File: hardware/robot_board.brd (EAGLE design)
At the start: 92.7 x 72.1 mm, 113 parts, among them J1 POWER_JACKPTH, U2 FT232RLSSOP

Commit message: check in library and restructured directories
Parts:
- removed U$4: MC74HC164, r_cubed:TSSOP-14
- removed U2: FT232RLSSOP, SparkFun-DigitalIC:SSOP28DB
- added R45, R46: (no value), resistor:R1206
- added U1: FT232RL-BASICSSOP, SparkFun-DigitalIC:SSOP28DB
- moved D24 2.84 mm to (33.0, 22.9)
- turned U17 to 270 degrees
- renumbered U$13 to U13, U$14 to U14, U$15 to U15, U$16 to U16, U$17 to U17, U$18 to U18, U$5 to U5, U$6 to U6
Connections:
- removed net N$28: U$4.9
- removed net N$29: U$4.1, U$4.2
- removed net N$32: U$4.8
- removed net V+: U$12.8
- removed net VCC: U2.20
- new net AOUT1: U$19.L, U$21.2
- new net AOUT2: U$19.R, U$21.4
- new net BOUT1: U$20.L, U$21.7
- new net BOUT2: U$20.R, U$21.5
- new net GND1: U1.7
- new net GND2: U1.18
- new net GND3: U1.21
- new net MAIN_PWR: C3.+, D25.A, JP6.1, JP6.2, JP6.3, JP6.4, R27.1, R31.2, U$3.P$1, U$3.P$3, U$9.2, U13.P$5, U13.P$6, U16.8, U5.P$4, U6.P$4
- new net N$52: R45.1, R46.2, U17.55
- net 5V: now also U13.P$1; no longer C3.+, D25.A, JP6.1, JP6.2, JP6.3, JP6.4, R27.1, R31.2, U$11.8, U$3.P$1, U$3.P$3, U$4.14, U$9.2, U13.P$5, U16.8, U5.P$4, U6.P$4
- net AGND: now also U1.25; no longer U2.25
- net GND: now also R46.1, U16.5, U16.6; no longer U$4.7, U2.18, U2.21, U2.7
- net LCD0: no longer U$4.3
- net LCD1: no longer U$4.4
- net LCD2: no longer U$4.5
- net LCD3: no longer U$4.6
- net LCD4: no longer U$4.10
- net LCD5: no longer U$4.11
- net LCD6: no longer U$4.12
- net LCD7: no longer U$4.13
- net N$1: now also U1.16; no longer U2.16
- net N$2: now also U1.15; no longer U2.15
- net USB_5V: now also U1.20
- net VCCIO: now also U1.4; no longer U2.4
- net VIN_F: now also R33.2, R45.2, U$11.8, U$12.8
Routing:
- net MAIN_PWR: track 0.00 -> 7.62 mm
- net 5V: track 7.62 -> 0.00 mm
- net N$29: track 0.63 -> 0.00 mm

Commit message: updated schematic
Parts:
- removed U$10: 1206PPTC_FUSE, jseng:R1206
- removed U15: DMP2035U, jseng:SOT23
- added D26, D27, D28, D29: (no value), SparkFun-DiscreteSemi:SOT23-3
- added F2: 1206PPTC_FUSE, jseng:R1206
- added R47, R48, R49, R50: 220, resistor:R1206
- added U2: NCP380, jseng:TSOP-5
- R30, R31, R32, R33, R34, R42: value (none) -> 10K
- U$2: value NCP380 -> SIA907EDJT; device jseng:TSOP-5 -> jseng:SC70T
- moved U$2 22.9 mm to (8.89, 21.6), turned to 0 degrees
- moved R43 12.5 mm to (35.6, 52.1), turned to 90 degrees
- moved JP3 5.08 mm to (10.2, 62.2)
- moved JP7 5.08 mm to (10.2, 67.3)
- moved U13 2.54 mm to (8.89, 15.2)
- moved U1 2.54 mm to (16.5, 45.7)
- moved F1 1.80 mm to (19.1, 34.3)
- moved U18 1.80 mm to (27.9, 50.8), turned to 180 degrees
- moved U17 1.27 mm to (68.6, 36.8)
- renumbered U$12 to U12, U$3 to U3, U$7 to U7, U$8 to U8
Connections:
- removed net AGND: U1.25
- removed net GND1: U1.7
- removed net GND2: U1.18
- removed net GND3: U1.21
- new net N$28: U$2.P$3, U$2.P$6
- new net N$29: D26.3, R47.1
- new net N$32: D27.3, R48.1
- new net N$53: D28.3, R49.1
- new net N$54: D29.3, R50.1
- new net SERVO0: JP3.1, R47.2
- new net SERVO1: JP3.2, R48.2
- new net SERVO2: JP3.3, R49.2
- new net SERVO3: JP3.4, R50.2
- net 5V: now also U13.P$10, U2.P$4, U2.P$6; no longer U$2.P$4, U$2.P$6
- net 5V_UC: now also U2.P$1; no longer U$2.P$1
- net GND: now also D26.1, D27.1, D28.1, D29.1, U1.18, U1.21, U1.25, U1.7, U2.P$5; no longer U$2.P$5
- net MAIN_PWR: now also U13.P$7, U13.P$8
- net N$27: now also F2.1; no longer U$10.1
- net N$31: now also U2.P$2; no longer U$2.P$2
- net USBGATE: now also U$2.P$2, U$2.P$5; no longer U15.1
- net USB_5V: now also F2.2, U$2.P$1; no longer U$10.2, U15.3
- net VIN_F: now also U$2.P$4; no longer U15.2
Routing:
- net MAIN_PWR: track 7.62 -> 0.00 mm
- net GND: track 16.7 -> 9.05 mm
- net N$26: track 2.80 -> 0.21 mm

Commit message: update libraries
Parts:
- removed U$21: DRV8833, jseng:TSSOP16
- added U$3: NRSINDUCTOR, jseng:TAIYO-NRS
- added U$4, U$5: DRV8839, jseng:PWSON-N12
- moved R34 10.2 mm to (20.3, 12.7), turned to 90 degrees
- moved R47 6.35 mm to (3.81, 57.1)
- moved U$20 5.08 mm to (22.9, 64.8), turned to 180 degrees
- moved R48 5.08 mm to (7.62, 57.1)
- moved U$19 5.08 mm to (33.0, 64.8), turned to 180 degrees
- moved R49 3.81 mm to (11.4, 57.1)
- moved R50 2.54 mm to (15.2, 57.1)
- moved R42 1.27 mm to (16.5, 12.7)
- moved U13 1.27 mm to (8.89, 16.5)
- moved R29 1.27 mm to (11.4, 25.4)
- moved U$2 1.27 mm to (8.89, 22.9)
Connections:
- new net N$55: U$3.P$2, U13.P$2
- new net N$56: U$3.P$1, U13.P$4
- new net N$58: U$4.P$1, U$4.P$2
- new net N$61: U$5.P$1, U$5.P$2
- net 5V: now also U$4.P$7, U$4.P$8, U$5.P$7, U$5.P$8
- net AOUT1: now also U$4.P$3; no longer U$21.2
- net AOUT2: now also U$4.P$4; no longer U$21.4
- net BOUT1: now also U$5.P$3; no longer U$21.7
- net BOUT2: now also U$5.P$4; no longer U$21.5
- net GND: now also U$4.P$5, U$4.P$6, U$5.P$5, U$5.P$6; no longer U$21.13

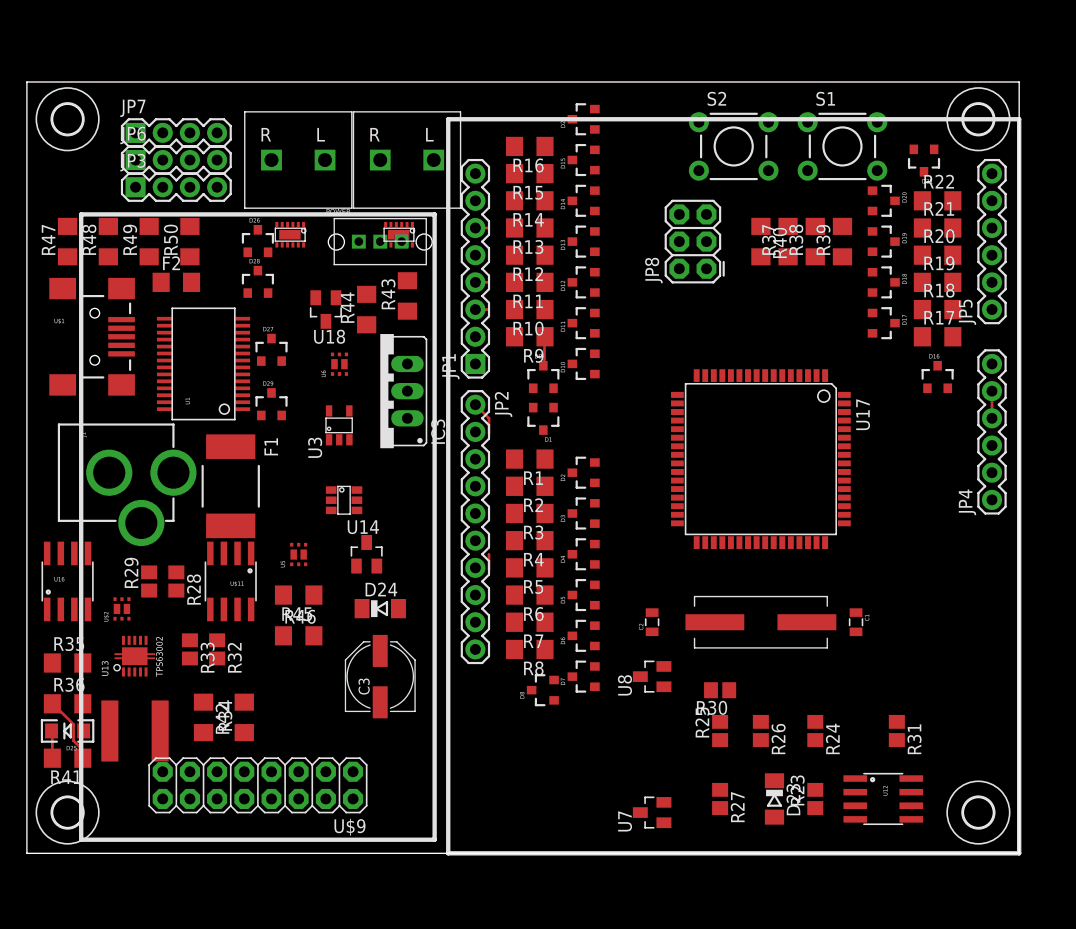
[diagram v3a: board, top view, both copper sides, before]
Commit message: added accelerometer device
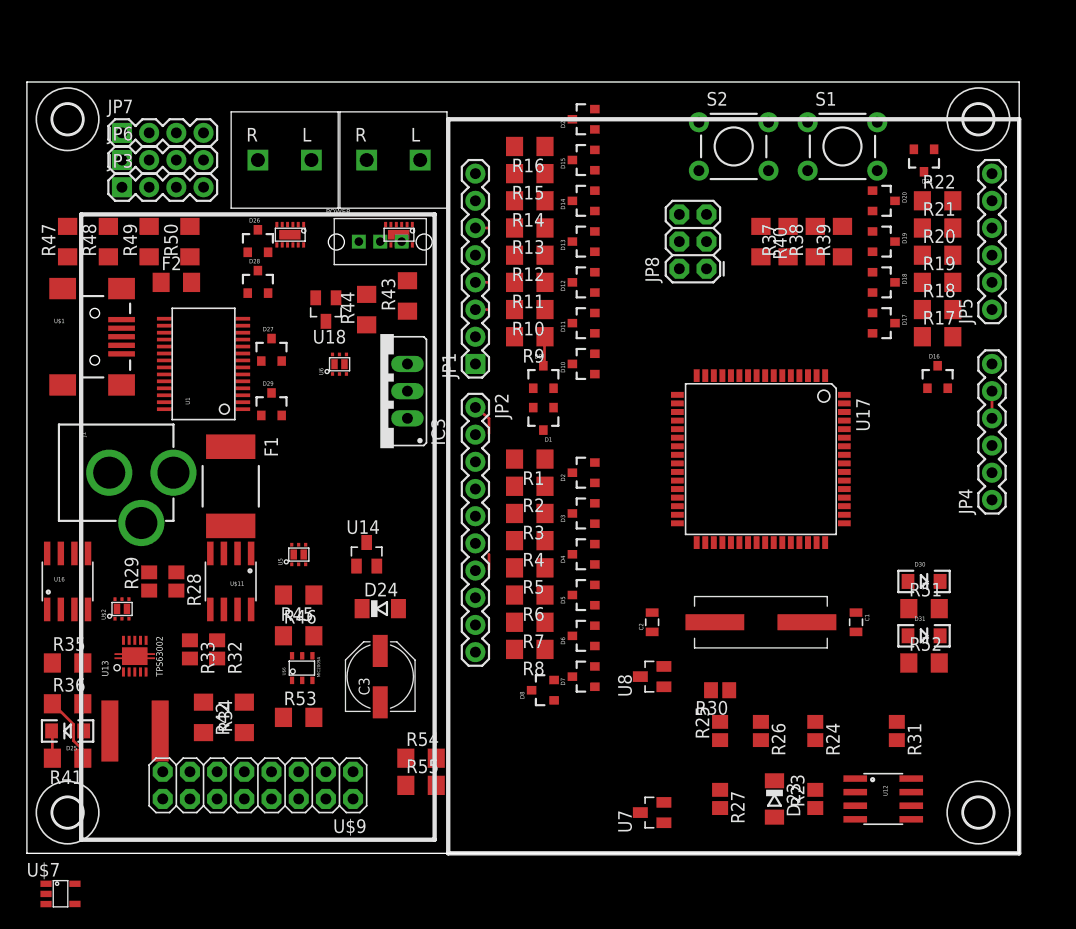
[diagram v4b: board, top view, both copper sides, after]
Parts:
- removed U2: NCP380, jseng:TSOP-5
- removed U3: TLV70233DBVR, jseng:SOT-23-5
- added D30: GREEN, SparkFun-LED:LED-1206
- added D31: YELLOW, SparkFun-LED:LED-1206
- added R51, R52: 330, resistor:R1206
- added R53: 1.5K, resistor:R1206
- added R54: 10K, resistor:R1206
- added R55: 1K, resistor:R1206
- added U$6: MIC2009A, jseng:SOT23-M5
- added U$7: TLV70233, jseng:SOT-23-5
- D23: value 2.7V -> 2.1V
- D25: value GREEN -> POWER
- R41: value (none) -> 330
- moved U$19 1.27 mm to (31.8, 64.8)
- moved JP3 1.27 mm to (8.89, 62.2)
- moved JP6 1.27 mm to (8.89, 64.8)
- moved JP7 1.27 mm to (8.89, 67.3)
- moved U$20 1.27 mm to (21.6, 64.8)
- moved JP2 0.25 mm to (41.9, 41.7)
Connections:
- net 10 renamed D10
- net 11 renamed D11
- net 12 renamed D12
- net 13 renamed D13
- net 2.7V renamed 2.1V
- net 8 renamed D8
- net 9 renamed D9
- net N$20 renamed D7_IN
- net N$29 renamed SERVO0_IN
- net N$32 renamed SERVO1_IN
- net N$5 renamed D8_IN
- net N$53 renamed SERVO2_IN
- net N$54 renamed SERVO3_IN
- net N$6 renamed D9_IN
- removed net N$10: D6.3, R6.1
- removed net N$11: D7.3, R7.1
- removed net N$12: D8.3, R8.1
- removed net N$13: D9.3, R9.1
- removed net N$14: D10.3, R10.1
- removed net N$15: D11.3, R11.1
- removed net N$16: D12.3, R12.1
- removed net N$17: D13.3, R13.1
- removed net N$18: D14.3, R14.1
- removed net N$19: D15.3, R15.1
- removed net N$21: D16.3, R17.1
- removed net N$22: D17.3, R18.1
- removed net N$23: D18.3, R19.1
- removed net N$24: D19.3, R20.1
- removed net N$25: D20.3, R21.1
- removed net N$26: D21.3, R22.1
- removed net N$31: U2.P$2
- removed net N$58: U$4.P$1, U$4.P$2
- removed net N$61: U$5.P$1, U$5.P$2
- removed net N$7: D3.3, R3.1
- removed net N$8: D4.3, R4.1
- removed net N$9: D5.3, R5.1
- new net A0_IN: D16.3, R17.1, U17.61
- new net A1_IN: D17.3, R18.1, U17.60
- new net A2_IN: D18.3, R19.1, U17.59
- new net A3_IN: D19.3, R20.1, U17.58
- new net A4_IN: D20.3, R21.1, U17.57
- new net A5_IN: D21.3, R22.1, U17.56
- new net D0_IN: D9.3, R9.1, U17.2
- new net D1_IN: D10.3, R10.1, U17.3
- new net D2_IN: D11.3, R11.1, U17.4
- new net D3_IN: D12.3, R12.1, U17.5
- new net D4_IN: D13.3, R13.1, U17.8
- new net D5_IN: D14.3, R14.1, U17.15
- new net D6_IN: D15.3, R15.1, U17.16
- new net LED0: D30.A, U17.33
- new net LED1: D31.A, U17.34
- new net M0_DIR0: U$4.P$9, U17.29
- new net M0_DIR1: U$4.P$11, U17.30
- new net M0_EN: U$4.P$10, U$4.P$12, U17.14
- new net M1_DIR0: U$5.P$9, U17.31
- new net M1_DIR1: U$5.P$11, U17.32
- new net M1_EN: U$5.P$10, U$5.P$12, U17.17
- new net N$5: R53.2, U$6.P$5
- new net N$57: D30.C, R51.2
- new net N$6: R55.2, U17.43
- new net N$62: D31.C, R52.2
- new net SCL_IN: D7.3, R7.1, U17.6
- new net SDA_IN: D8.3, R8.1, U17.7
- new net SS: D3.3, R3.1, U17.10
- net 3V3: now also U$7.P$4; no longer U3.P$4
- net 5V: now also U$6.P$1; no longer U2.P$4, U2.P$6
- net 5V_UC: no longer U2.P$1
- net A0: no longer U17.61
- net A1: no longer U17.60
- net A2: no longer U17.59
- net A3: no longer U17.58
- net A4: no longer U17.57
- net A5: no longer U17.56
- net AREF: now also U17.62
- net D0: no longer U17.2
- net D1: no longer U17.3
- net GND: now also R51.1, R52.1, R53.1, R54.1, U$7.P$2; no longer U2.P$5, U3.P$2
- net HIGH_5V_REG: now also U6.P$6; no longer U6.P$1
- net MAIN_PWR: now also U$7.P$1, U$7.P$3, U5.P$3, U6.P$3; no longer U3.P$1, U3.P$3, U5.P$4, U6.P$4
- net MISO: now also D5.3, R5.1, U17.13
- net MOSI: now also D4.3, R4.1, U17.12
- net N$28: now also U$2.P$1, U$2.P$4; no longer U$2.P$3, U$2.P$6
- net N$42: now also U6.P$1, U6.P$4; no longer U6.P$3, U6.P$6
- net N$44: now also U5.P$1, U5.P$4; no longer U5.P$3, U5.P$6
- net SCK: now also D6.3, R6.1, U17.11
- net USB_5V: now also R54.2, R55.1, U$2.P$6; no longer U$2.P$1
- net VIN_F: now also U$2.P$3, U$4.P$1, U$4.P$2, U$5.P$1, U$5.P$2, U5.P$6; no longer U$2.P$4, U5.P$1
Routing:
- net N$13: track 2.80 -> 0.00 mm
- net D0_IN: track 0.00 -> 2.80 mm

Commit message: changed board size and added gyro interrupt
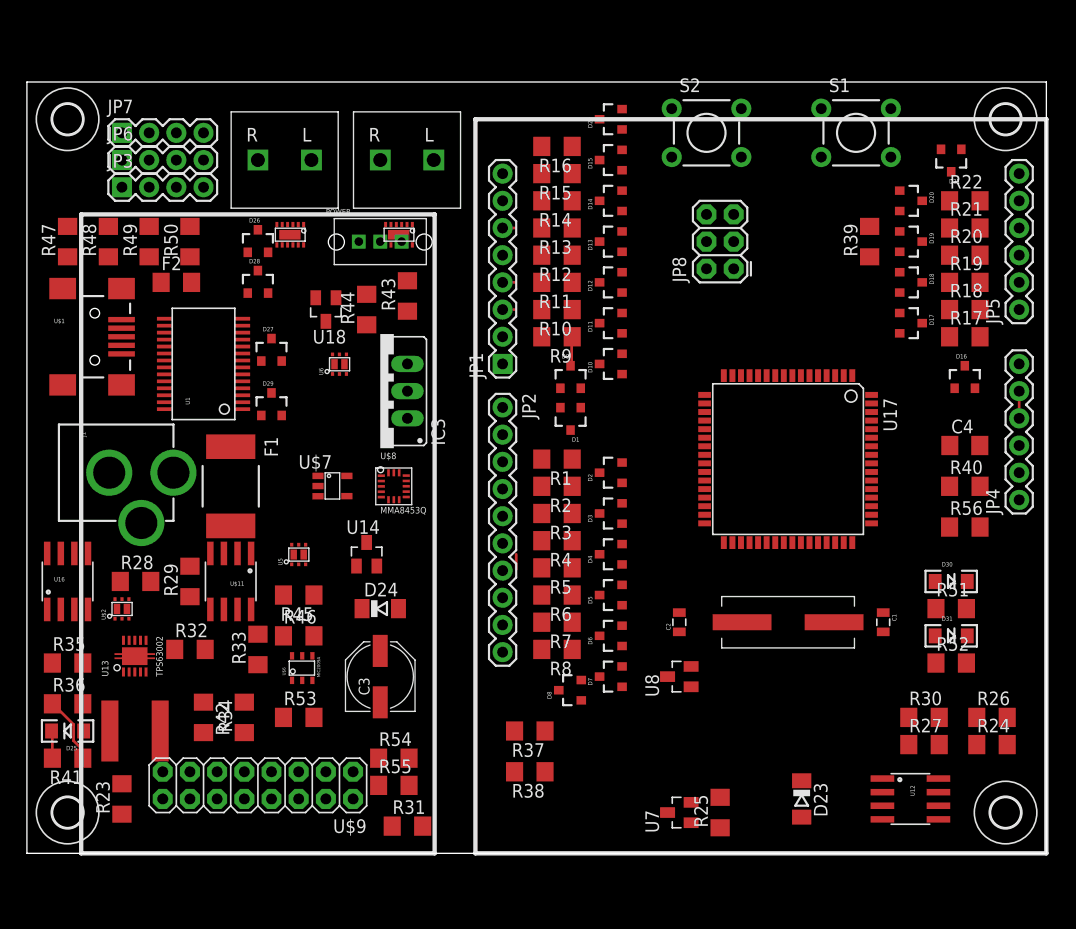
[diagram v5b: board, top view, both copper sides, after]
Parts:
- added C4: .1uF, resistor:C1206
- added R56: 1K, resistor:R1206
- added U$8: MMA8453Q, jseng:QFN-COL
- R23, R24, R25, R26, R27: device resistor:R0805 -> resistor:R1206
- R28: value 86.6K -> (none); device resistor:R0805 -> resistor:R1206
- R29: value 100K -> (none); device resistor:R0805 -> resistor:R1206
- R30, R31, R32, R33: value 10K -> (none); device resistor:R0805 -> resistor:R1206
- R37, R38: value 1k -> 4.7K
- R40: value 1k -> 10K
- moved R23 64.8 mm to (8.89, 5.08)
- moved R38 56.3 mm to (47.0, 7.62), turned to 180 degrees
- moved R37 51.7 mm to (47.0, 11.4), turned to 180 degrees
- moved R31 46.6 mm to (35.6, 2.54), turned to 0 degrees
- moved U$7 45.8 mm to (26.7, 33.0)
- moved R40 29.8 mm to (87.6, 34.3), turned to 0 degrees
- moved R26 21.6 mm to (90.2, 12.7), turned to 0 degrees
- moved R27 19.7 mm to (83.8, 10.2), turned to 0 degrees
- moved R30 19.2 mm to (83.8, 12.7), turned to 0 degrees
- moved R24 16.6 mm to (90.2, 10.2), turned to 0 degrees
- moved R25 7.62 mm to (64.8, 3.81)
- moved R33 6.35 mm to (21.6, 19.1), turned to 90 degrees
- moved R28 3.81 mm to (10.2, 25.4), turned to 0 degrees
- moved R29 3.81 mm to (15.2, 25.4)
- moved S2 2.84 mm to (63.5, 67.3)
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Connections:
- removed net N$37: JP8.4, R40.1
- removed net N$49: JP8.3, R38.2
- removed net N$50: JP8.1, R37.2
- new net DTR: C4.1, U1.2
- new net GYRO_INT: U$8.P$11, U17.26
- new net LCD_E: U17.19
- new net LCD_RS: U17.18
- new net N$7: JP4.1, R56.2
- new net SW1: S2.3, S2.4
- net 2.1V: now also R23.1; no longer R27.2
- net 3V3: now also R37.2, R38.2, U$8.P$1, U$8.P$14, U$8.P$15, U$8.P$16
- net 3V3_OUT: now also R27.2; no longer R24.2
- net 5VREG_SW: now also R33.1; no longer R32.1
- net 5VREG_SWO: now also R32.1; no longer R33.1
- net 5V_OUT: now also R24.2; no longer R26.2
- net 5V_UC: now also R40.1
- net D11: now also JP8.4
- net D12: now also JP8.1
- net D13: now also JP8.3
- net GND: now also R26.1, R28.1, R31.1, S2.1, S2.2, U$8.P$10, U$8.P$12, U$8.P$13, U$8.P$5, U$8.P$7, U$8.P$8; no longer R23.1, R25.1, R29.1
- net LCD0: now also U17.51
- net LCD1: now also U17.50
- net LCD2: now also U17.49
- net LCD3: now also U17.48
- net LCD4: now also U17.47
- net LCD5: now also U17.46
- net LCD6: now also U17.45
- net LCD7: now also U17.44
- net MAIN_PWR: now also R23.2, R25.2; no longer R27.1, R31.2
- net MISO: no longer R37.1
- net MOSI: no longer R40.2
- net N$3: now also U17.23
- net N$30: now also R25.1; no longer R31.1
- net N$34: now also R24.1, R26.2; no longer R25.2, R26.1
- net N$35: now also R28.2, R29.1; no longer R28.1, R29.2
- net N$38: now also R27.1, R31.2; no longer R23.2, R24.1
- net N$4: now also U17.24
- net RESET: now also C4.2, R40.2, R56.1; no longer JP4.1
- net SCK: no longer R38.1
- net SCL_IN: now also R38.1, U$8.P$4
- net SDA_IN: now also R37.1, U$8.P$6
- net VIN_F: now also R29.2; no longer R28.2
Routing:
- net D8: track 3.05 -> 0.00 mm
- net D0: track 0.88 -> 0.00 mm
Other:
- board size 92.7 x 72.1 mm -> 95.2 x 72.1 mm

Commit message: modified overall layout
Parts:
- removed D24: 6V, diode:SOD80C
- removed U$1: USB-MINIB-5PIN, SparkFun-Connectors:USB-MINIB
- removed U$11: LM393, SparkFun-AnalogIC:SO08
- removed U$3: NRSINDUCTOR, jseng:TAIYO-NRS
- removed U13: TPS63002, jseng:10SON
- removed U14, U18: DMP2035U, jseng:SOT23
- removed U7, U8: DMP2035U-7, jseng:SOT23
- added C5: .1uF, resistor:C1206
- added JP9: USB-B, SparkFun-Connectors:USB-B-PTH
- added Q1, Q2: DMP2035U, jseng:SOT23
- added Q3, Q4: DMP2035U-7, jseng:SOT23
- added U11: LM393, SparkFun-AnalogIC:SO08
- moved R51 91.6 mm to (2.54, 59.7), turned to 270 degrees
- moved D30 88.4 mm to (2.54, 53.3), turned to 90 degrees
- moved J1 86.9 mm to (78.7, -1.27), turned to 0 degrees
- moved D31 86.2 mm to (2.54, 40.6), turned to 270 degrees
- moved R52 85.4 mm to (2.54, 34.3), turned to 90 degrees
- moved C1 81.8 mm to (7.62, 59.7)
- moved U16 75.0 mm to (78.7, 22.9)
- moved F1 74.0 mm to (90.2, 14.0), turned to 90 degrees
- moved D25 70.3 mm to (72.4, 26.7), turned to 90 degrees
- moved F2 70.1 mm to (71.1, 12.7), turned to 90 degrees
- moved R41 69.5 mm to (69.8, 30.5)
- moved Y1 66.6 mm to (16.5, 59.7), turned to 0 degrees
- moved R23 64.8 mm to (66.0, 35.6), turned to 180 degrees
- moved JP7 64.8 mm to (8.89, 2.54)
- moved R54 60.2 mm to (62.2, 62.2)
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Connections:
- removed net N$27: F2.1, U$1.VBUS
- removed net N$55: U$3.P$2, U13.P$2
- removed net N$56: U$3.P$1, U13.P$4
- removed net VCCIO: U1.4
- new net N$31: U$6.P$4
- new net N$8: C5.1, U$8.P$2
- new net N$9: F2.1, JP9.VBUS
- net 2.1V: now also U11.2, U11.5; no longer U$11.2, U$11.5
- net 3V3: now also Q4.3; no longer U8.3
- net 3V3_OUT: now also Q4.2; no longer U8.2
- net 5V: now also Q3.3, U$6.P$3; no longer U13.P$1, U13.P$10, U7.3
- net 5VREG_SW: now also U11.7; no longer U$11.7
- net 5VREG_SWO: now also U11.1, U11.6; no longer U$11.1, U$11.6
- net 5V_OUT: now also Q3.2; no longer U7.2
- net 5V_UC: now also U$6.P$6
- net GND: now also C5.2, JP9.GND, U$6.P$2, U11.4; no longer U$1.GND, U$11.4, U13.P$3, U13.P$9
- net MAIN_PWR: no longer U13.P$5, U13.P$6, U13.P$7, U13.P$8
- net N$1: now also JP9.D-; no longer U$1.D-
- net N$2: now also JP9.D+; no longer U$1.D+
- net N$30: now also Q3.1; no longer U7.1
- net N$33: now also Q1.3; no longer U14.3
- net N$35: now also U11.3; no longer U$11.3
- net N$36: now also Q1.1; no longer D24.A, U14.1
- net N$40: now also Q1.2, Q2.2; no longer D24.C, U14.2, U18.2
- net N$45: now also Q4.1; no longer U8.1
- net N$51: now also Q2.1; no longer U18.1
- net USB_5V: now also U1.4
- net VIN_F: now also Q2.3, U11.8; no longer U$11.8, U18.3
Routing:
- net GND: track 9.05 -> 2.54 mm
- net D0_IN: track 2.80 -> 0.00 mm
- net N$41: track 2.59 -> 0.00 mm
- net D13: track 1.42 -> 0.00 mm
- net D5: track 1.12 -> 2.54 mm
- net D3: track 1.12 -> 0.00 mm
- net D2: track 1.12 -> 0.00 mm
